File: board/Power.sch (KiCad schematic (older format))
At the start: 111 parts, among them CON1 BARREL_JACK, CON2 BARREL_JACK, P1 CONN_2, U12 TPS51200, U4 GBU15005-G, U6 TPS54560, U7 TPS53319, U8 TPS54625, U9 TPS54625

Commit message: Issue #9
Added DC blocking capacitors, VTTREF issue solved, 5V power common
connection issue solved
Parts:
- added C268, C269: 47UF, SM1210L, symbol C
- added D14: DIODESCH, DO-214AC(SMA), symbol DIODESCH
- added P27: ATX_POWER_SUPPLY, ~, symbol ATX_POWER_SUPPLY
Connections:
- wire segments 319 -> 334
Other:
- note added: "* R99 is the RF resister is used for selecting switching frequency of TPS53319, If left this pin open , the switching frequency will be 500Khz.Please refer Table 1 for more details."
- note added: "*DNP"
- note added: "Table 1 Resistor and Switching Frequency"

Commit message: s/UF/uF/gc
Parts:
- C133, C134, C135, C136, C138, C139, C140, C145, C156, C159, C162, C166, C168, C76, C78, C79, C81: value 10UF -> 10uF
- C137, C141, C148: value 1UF -> 1uF
- C142, C149, C150, C152, C153, C154, C155, C158, C80: value 0.1UF -> 0.1uF
- C146: value 0.001UF -> 0.001uF
- C147, C77: value 4.7UF -> 4.7uF
- C157, C160, C163: value 100UF -> 100uF
- C161, C164, C165, C167, C268, C269, C59, C61: value 47UF -> 47uF
- C72, C73, C74, C75: value 22UF -> 22uF

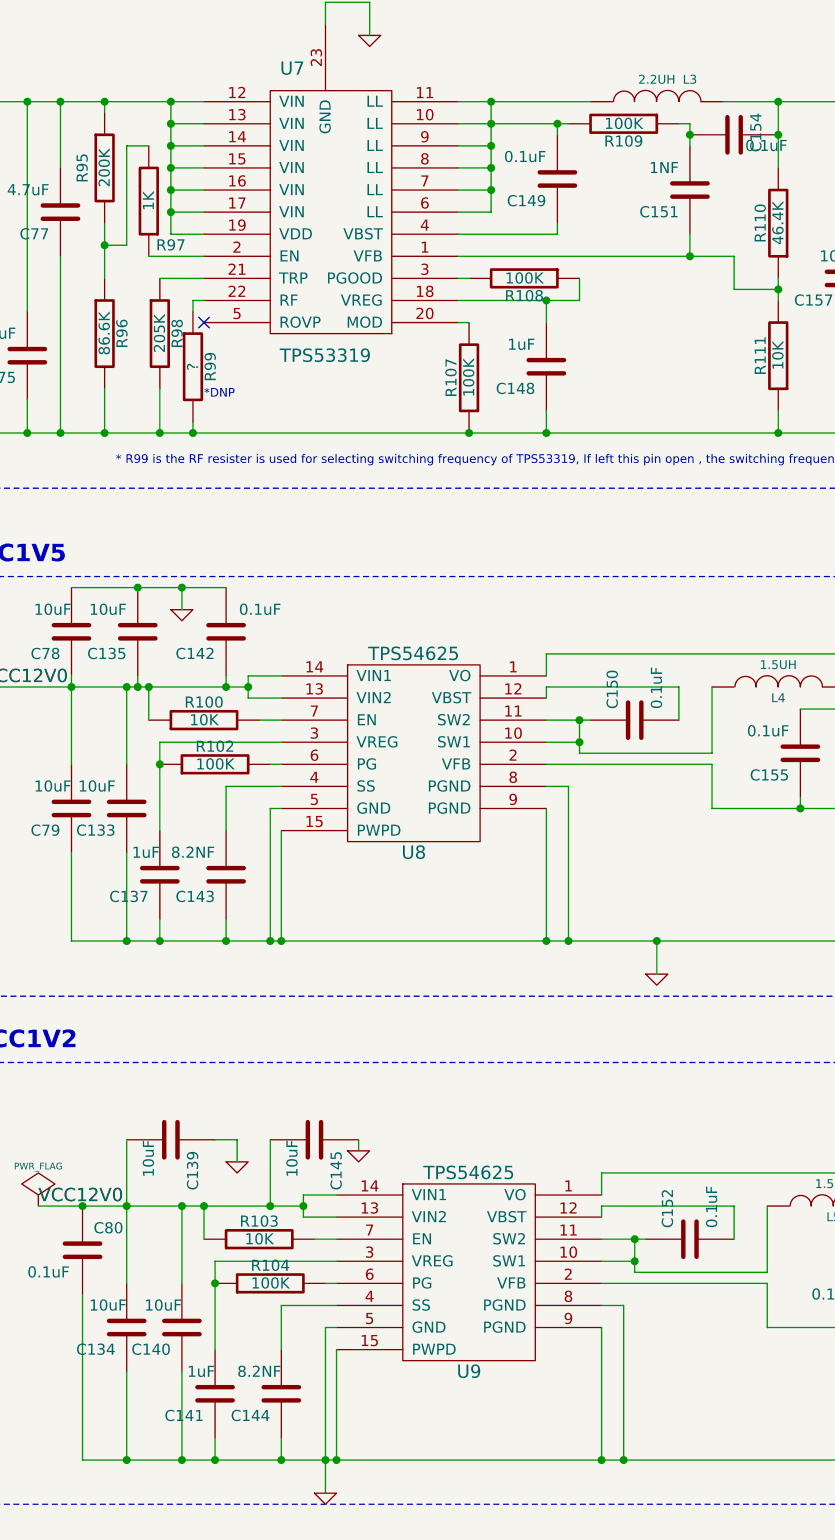
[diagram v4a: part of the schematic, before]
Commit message: s/NF/nF/gc
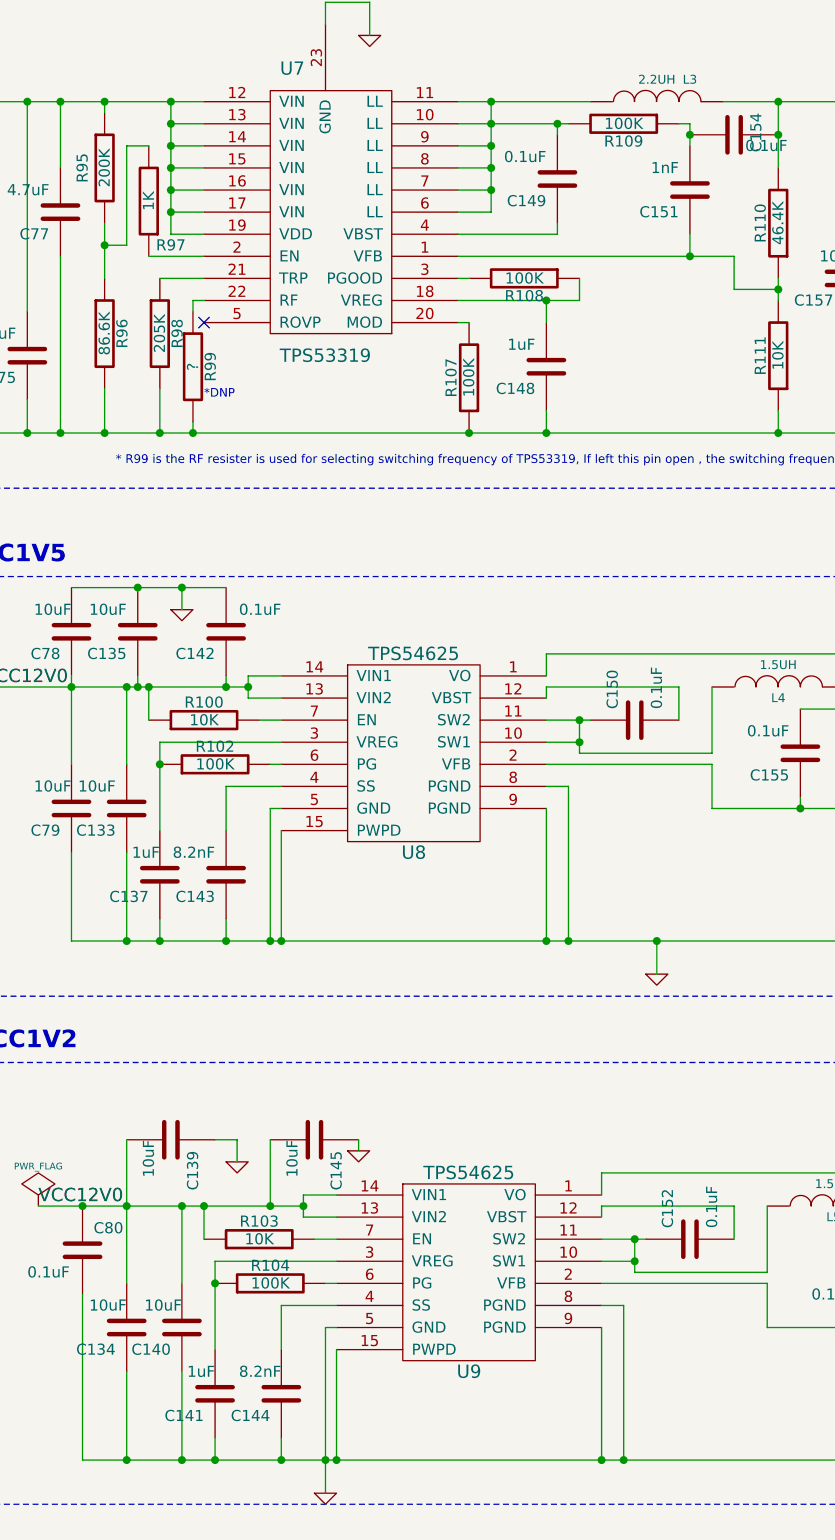
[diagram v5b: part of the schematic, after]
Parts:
- C143, C144: value 8.2NF -> 8.2nF
- C151: value 1NF -> 1nF
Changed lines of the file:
@@
 P 10850 4900
 F 0 "C143" H 10900 5000 50  0000 L CNN
-F 1 "8.2NF" H 10900 4800 50  0000 L CNN
+F 1 "8.2nF" H 10900 4800 50  0000 L CNN
 F 2 "SM0805" H 10850 4900 60  0001 C CNN
 F 3 "" H 10850 4900 60  0000 C CNN
@@
 P 11100 7250
 F 0 "C144" H 11150 7350 50  0000 L CNN
-F 1 "8.2NF" H 11100 7150 50  0000 L CNN
+F 1 "8.2nF" H 11100 7150 50  0000 L CNN
 F 2 "SM0805" H 11100 7250 60  0001 C CNN
 F 3 "" H 11100 7250 60  0000 C CNN
@@
 P 12950 1800
 F 0 "C151" H 13000 1900 50  0000 L CNN
-F 1 "1NF" H 13000 1700 50  0000 L CNN
+F 1 "1nF" H 13000 1700 50  0000 L CNN
 F 2 "SM0805" H 12950 1800 60  0001 C CNN
 F 3 "" H 12950 1800 60  0000 C CNN

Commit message: s/_Capa//gc
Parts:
- C60, C63, C65, R77, R78, R79: footprint SM0603_Capa -> SM0603
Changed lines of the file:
@@
 F 0 "C60" H 4400 4050 50  0000 L CNN
 F 1 "0.1uF" H 4350 3850 50  0000 L CNN
-F 2 "SM0603_Capa" H 4350 3950 60  0001 C CNN
+F 2 "SM0603" H 4350 3950 60  0001 C CNN
 F 3 "" H 4350 3950 60  0000 C CNN
 F 4 "No" H 4350 3950 60  0001 C CNN "Populate"
@@
 F 0 "R77" V 3230 4750 50  0000 C CNN
 F 1 "442K" V 3150 4750 50  0000 C CNN
-F 2 "SM0603_Capa" H 3150 4750 60  0001 C CNN
+F 2 "SM0603" H 3150 4750 60  0001 C CNN
 F 3 "" H 3150 4750 60  0000 C CNN
 F 4 "No" H 3150 4750 60  0001 C CNN "Populate"
@@
 F 0 "R78" V 3480 5050 50  0000 C CNN
 F 1 "92.3K" V 3400 5050 50  0000 C CNN
-F 2 "SM0603_Capa" H 3400 5050 60  0001 C CNN
+F 2 "SM0603" H 3400 5050 60  0001 C CNN
 F 3 "" H 3400 5050 60  0000 C CNN
 F 4 "No" H 3400 5050 60  0001 C CNN "Populate"
@@
 F 0 "R79" V 3730 5200 50  0000 C CNN
 F 1 "243K" V 3650 5200 50  0000 C CNN
-F 2 "SM0603_Capa" H 3650 5200 60  0001 C CNN
+F 2 "SM0603" H 3650 5200 60  0001 C CNN
 F 3 "" H 3650 5200 60  0000 C CNN
 F 4 "No" H 3650 5200 60  0001 C CNN "Populate"
@@
 F 0 "C63" H 4850 5300 50  0000 L CNN
 F 1 "6.2nF" H 4800 5100 50  0000 L CNN
-F 2 "SM0603_Capa" H 4800 5200 60  0001 C CNN
+F 2 "SM0603" H 4800 5200 60  0001 C CNN
 F 3 "" H 4800 5200 60  0000 C CNN
 F 4 "No" H 4800 5200 60  0001 C CNN "Populate"
@@
 F 0 "C65" H 5600 5550 50  0000 L CNN
 F 1 "4.7uF" H 5550 5350 50  0000 L CNN
-F 2 "SM0603_Capa" H 5550 5450 60  0001 C CNN
+F 2 "SM0603" H 5550 5450 60  0001 C CNN
 F 3 "" H 5550 5450 60  0000 C CNN
 F 4 "No" H 5550 5450 60  0001 C CNN "Populate"

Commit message: s/_Resistor//gc
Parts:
- R90, R91: footprint SM0603_Resistor -> SM0603
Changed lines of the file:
@@
 F 0 "R90" V 7030 4800 50  0000 C CNN
 F 1 "143K" V 6950 4800 50  0000 C CNN
-F 2 "SM0603_Resistor" H 6950 4800 60  0001 C CNN
+F 2 "SM0603" H 6950 4800 60  0001 C CNN
 F 3 "" H 6950 4800 60  0000 C CNN
 F 4 "No" H 6950 4800 60  0001 C CNN "Populate"
@@
 F 0 "R91" V 7030 5450 50  0000 C CNN
 F 1 "10.2K" V 6950 5450 50  0000 C CNN
-F 2 "SM0603_Resistor" H 6950 5450 60  0001 C CNN
+F 2 "SM0603" H 6950 5450 60  0001 C CNN
 F 3 "" H 6950 5450 60  0000 C CNN
 F 4 "No" H 6950 5450 60  0001 C CNN "Populate"

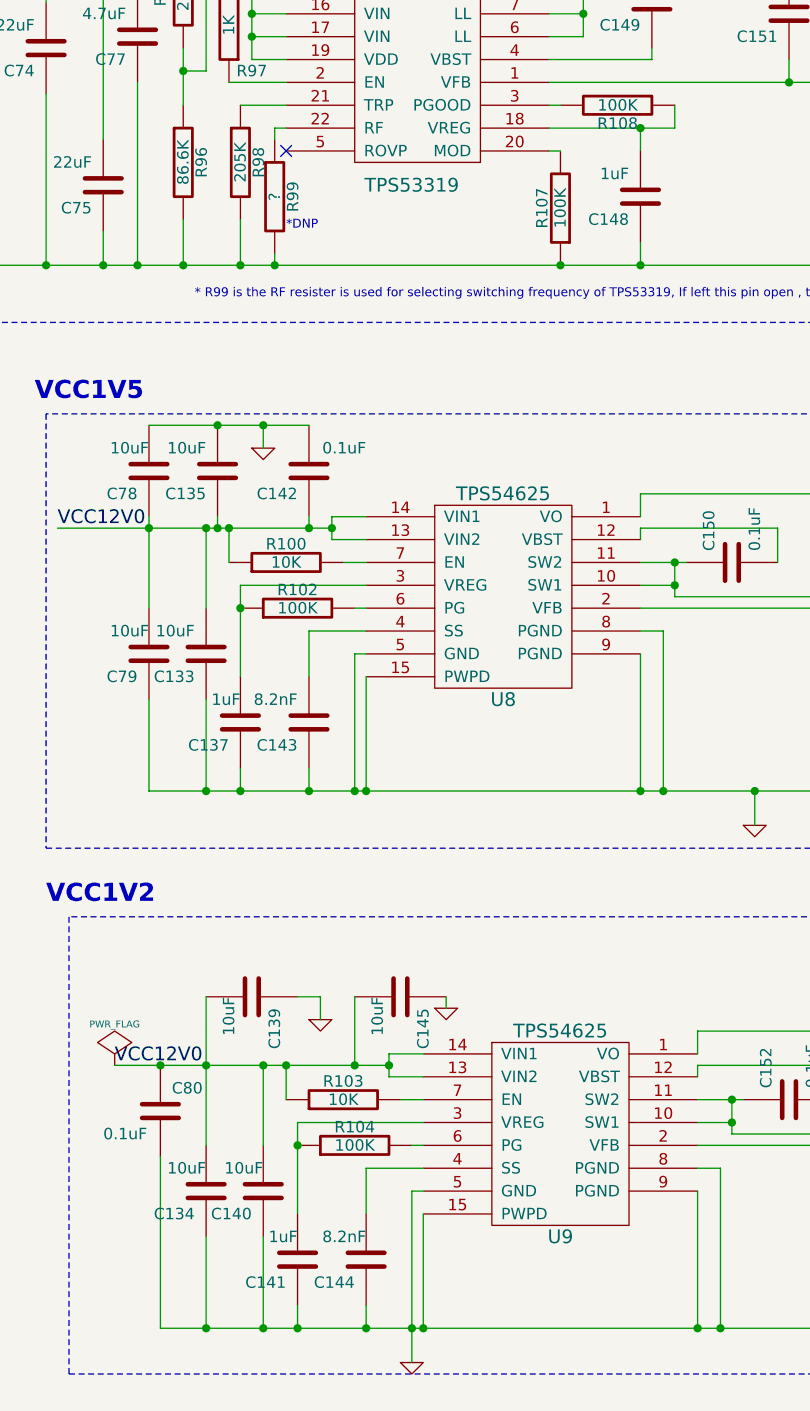
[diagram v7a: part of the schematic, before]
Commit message: s/1uF/1.0uF/gc
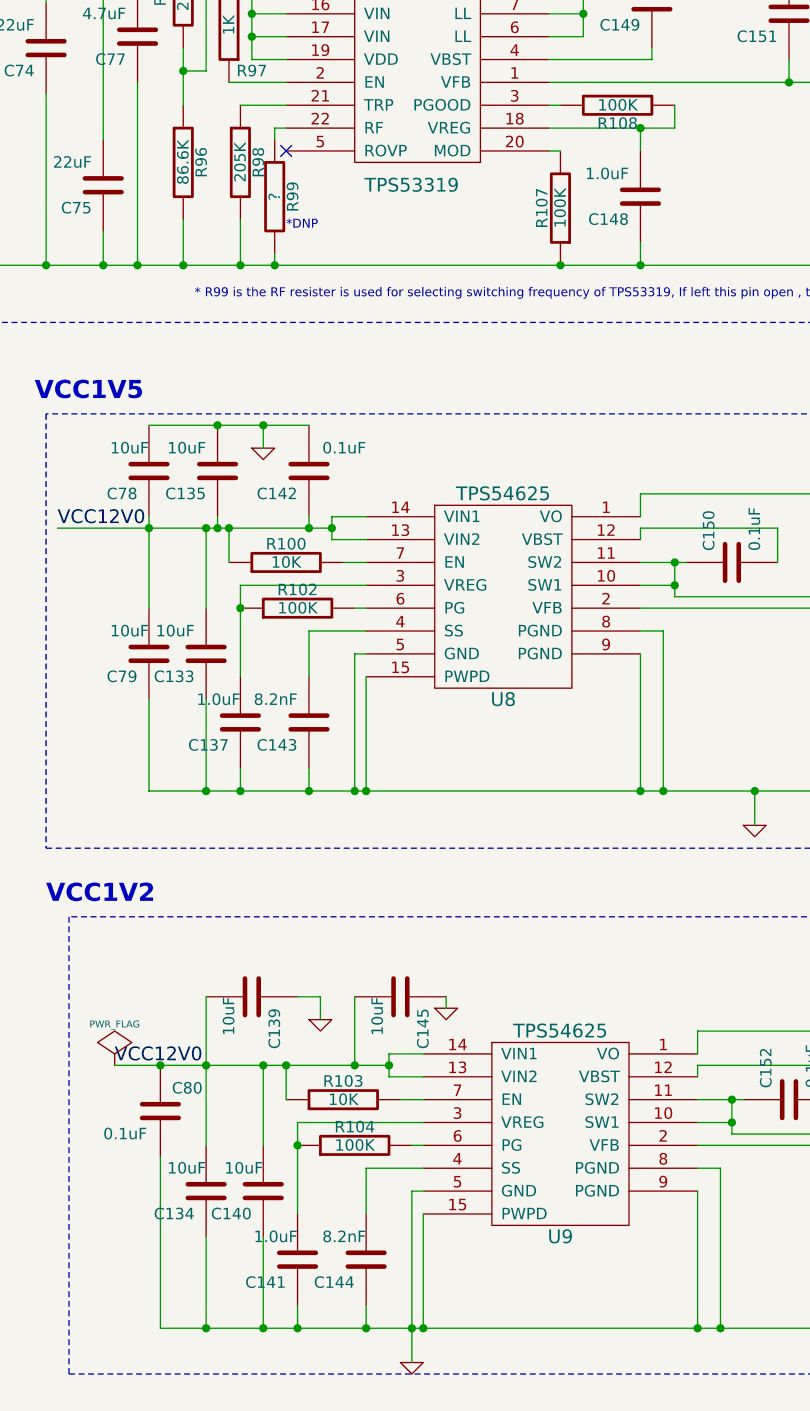
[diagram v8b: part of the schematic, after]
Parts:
- C137, C141, C148: value 1uF -> 1.0uF
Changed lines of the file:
@@
 P 10550 4900
 F 0 "C137" H 10600 5000 50  0000 L CNN
-F 1 "1uF" H 10550 4800 50  0000 L CNN
+F 1 "1.0uF" H 10550 4800 50  0000 L CNN
 F 2 "SM0603" H 10550 4900 60  0001 C CNN
 F 3 "" H 10550 4900 60  0000 C CNN
@@
 P 10800 7250
 F 0 "C141" H 10850 7350 50  0000 L CNN
-F 1 "1uF" H 10800 7150 50  0000 L CNN
+F 1 "1.0uF" H 10800 7150 50  0000 L CNN
 F 2 "SM0603" H 10800 7250 60  0001 C CNN
 F 3 "" H 10800 7250 60  0000 C CNN
@@
 P 12300 2600
 F 0 "C148" H 12350 2700 50  0000 L CNN
-F 1 "1uF" H 12350 2500 50  0000 L CNN
+F 1 "1.0uF" H 12350 2500 50  0000 L CNN
 F 2 "SM0603" H 12300 2600 60  0001 C CNN
 F 3 "" H 12300 2600 60  0000 C CNN
